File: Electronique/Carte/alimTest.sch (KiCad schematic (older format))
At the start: 20 parts

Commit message: Electronique
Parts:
- R4: value 1.7k -> 1.8k
- R5: value 2.1k -> 2.4k
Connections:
- net +15V renamed +20V
- net +15V_P renamed +20V_P
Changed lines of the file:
@@
 P 3150 5250
 F 0 "R4" V 3230 5250 50  0000 C CNN
-F 1 "1.7k" V 3150 5250 50  0000 C CNN
+F 1 "1.8k" V 3150 5250 50  0000 C CNN
 F 2 "Discret:R4" V 3080 5250 50  0001 C CNN
 F 3 "" H 3150 5250 50  0001 C CNN
@@
 P 5250 5250
 F 0 "R5" V 5330 5250 50  0000 C CNN
-F 1 "2.1k" V 5250 5250 50  0000 C CNN
+F 1 "2.4k" V 5250 5250 50  0000 C CNN
 F 2 "Discret:R4" V 5180 5250 50  0001 C CNN
 F 3 "" H 5250 5250 50  0001 C CNN
@@
 $EndComp
 Text GLabel 5700 4650 1    60   Input ~ 0
-+15V
++20V
 Text GLabel 4350 5250 0    60   Input ~ 0
 GND
 Text GLabel 5700 5500 3    60   Input ~ 0
-+15V_P
++20V_P
 Wire Wire Line
 	4350 5250 4650 5250

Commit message: kicadFinal
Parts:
- R5: value 2.4k -> 1.8k
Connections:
- net +20V renamed +15V
- net +20V_P renamed +15V_P
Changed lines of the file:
@@
 EESchema Schematic File Version 2
-LIBS:1A_cdfr2017
-LIBS:1A_cdfr2017-rescue
-LIBS:1A_cdfr2017-cache
 LIBS:power
 LIBS:device
@@
 LIBS:mcp2562
 LIBS:dsn2596
+LIBS:1A_cdfr2017
+LIBS:central-cache
+LIBS:central-rescue
 LIBS:carte_1A_cdfr2018-cache
 EELAYER 25 0
@@
 $Descr A4 11693 8268
 encoding utf-8
-Sheet 2 3
+Sheet 2 4
 Title ""
 Date ""
@@
 	3050 3750 3450 3750
 $Comp
-L PWR_FLAG #FLG06
+L PWR_FLAG #FLG028
 U 1 1 591A32A2
 P 3750 3650
-F 0 "#FLG06" H 3750 3725 50  0001 C CNN
+F 0 "#FLG028" H 3750 3725 50  0001 C CNN
 F 1 "PWR_FLAG" H 3750 3800 50  0000 C CNN
 F 2 "" H 3750 3650 50  0001 C CNN
@@
 	5150 3750 5550 3750
 $Comp
-L PWR_FLAG #FLG07
+L PWR_FLAG #FLG029
 U 1 1 5A64E1BA
 P 5850 3650
-F 0 "#FLG07" H 5850 3725 50  0001 C CNN
+F 0 "#FLG029" H 5850 3725 50  0001 C CNN
 F 1 "PWR_FLAG" H 5850 3800 50  0000 C CNN
 F 2 "" H 5850 3650 50  0001 C CNN
@@
 	7250 3750 7650 3750
 $Comp
-L PWR_FLAG #FLG08
+L PWR_FLAG #FLG030
 U 1 1 5A64E3A9
 P 7950 3650
-F 0 "#FLG08" H 7950 3725 50  0001 C CNN
+F 0 "#FLG030" H 7950 3725 50  0001 C CNN
 F 1 "PWR_FLAG" H 7950 3800 50  0000 C CNN
 F 2 "" H 7950 3650 50  0001 C CNN
@@
 	3050 5450 3450 5450
 $Comp
-L PWR_FLAG #FLG?
+L PWR_FLAG #FLG031
 U 1 1 5AC0B972
 P 3750 5350
-F 0 "#FLG?" H 3750 5425 50  0001 C CNN
+F 0 "#FLG031" H 3750 5425 50  0001 C CNN
 F 1 "PWR_FLAG" H 3750 5500 50  0000 C CNN
 F 2 "" H 3750 5350 50  0001 C CNN
@@
 P 5250 5250
 F 0 "R5" V 5330 5250 50  0000 C CNN
-F 1 "2.4k" V 5250 5250 50  0000 C CNN
+F 1 "1.8k" V 5250 5250 50  0000 C CNN
 F 2 "Discret:R4" V 5180 5250 50  0001 C CNN
 F 3 "" H 5250 5250 50  0001 C CNN
@@
 $EndComp
 Text GLabel 5700 4650 1    60   Input ~ 0
-+20V
++15V
 Text GLabel 4350 5250 0    60   Input ~ 0
 GND
 Text GLabel 5700 5500 3    60   Input ~ 0
-+20V_P
++15V_P
 Wire Wire Line
 	4350 5250 4650 5250
@@
 	5150 5450 5550 5450
 $Comp
-L PWR_FLAG #FLG?
+L PWR_FLAG #FLG032
 U 1 1 5AC0BAE9
 P 5850 5350
-F 0 "#FLG?" H 5850 5425 50  0001 C CNN
+F 0 "#FLG032" H 5850 5425 50  0001 C CNN
 F 1 "PWR_FLAG" H 5850 5500 50  0000 C CNN
 F 2 "" H 5850 5350 50  0001 C CNN

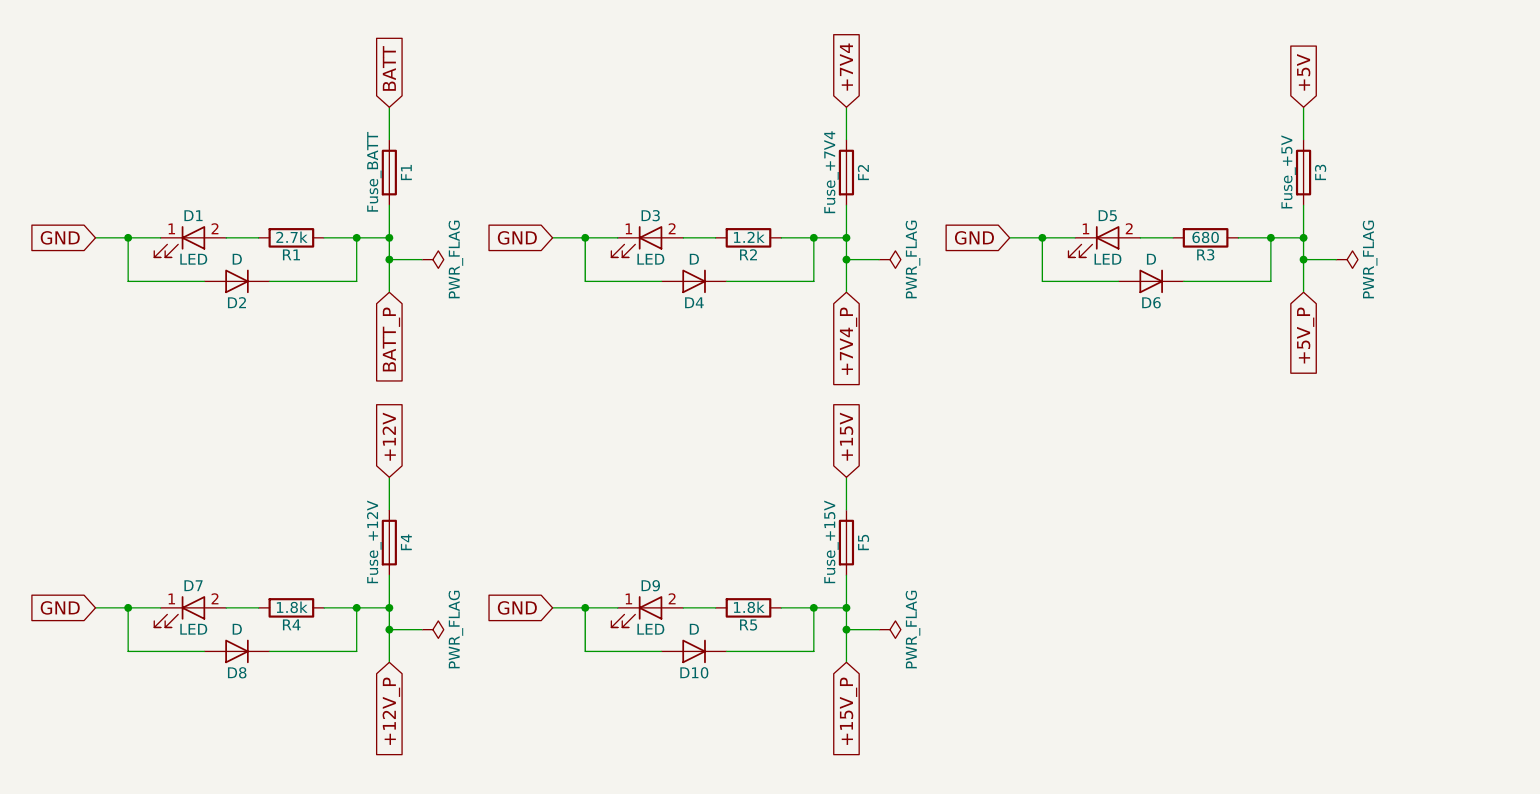
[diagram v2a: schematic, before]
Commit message: rapide corretion des empreintes pour les servos
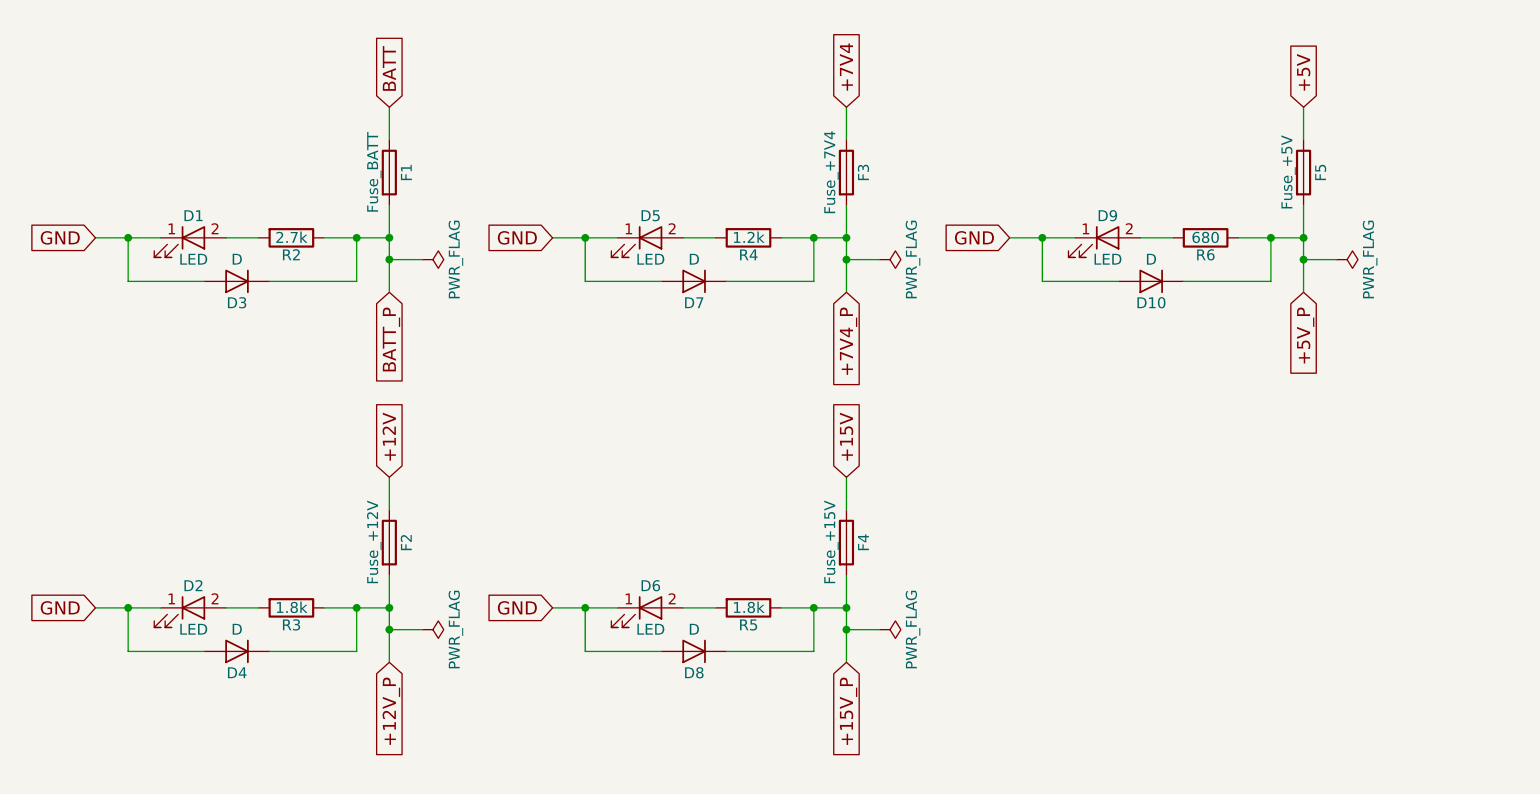
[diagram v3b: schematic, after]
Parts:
- renumbered D6 to D10, D7 to D2, D2 to D3, D8 to D4, D3 to D5, D9 to D6, D4 to D7, D10 to D8, D5 to D9, F4 to F2, F2 to F3, F5 to F4, F3 to F5, R1 to R2, R4 to R3, R2 to R4, R3 to R6
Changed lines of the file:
@@
 $EndComp
 $Comp
-L R R1
+L R R2
 U 1 1 5916B62D
 P 3150 3550
-F 0 "R1" V 3230 3550 50  0000 C CNN
+F 0 "R2" V 3230 3550 50  0000 C CNN
 F 1 "2.7k" V 3150 3550 50  0000 C CNN
 F 2 "Discret:R4" V 3080 3550 50  0001 C CNN
@@
 Connection ~ 3600 3550
 $Comp
-L D D2
+L D D3
 U 1 1 5916B9FB
 P 2900 3750
-F 0 "D2" H 2900 3850 50  0000 C CNN
+F 0 "D3" H 2900 3850 50  0000 C CNN
 F 1 "D" H 2900 3650 50  0000 C CNN
 F 2 "Discret:D4" H 2900 3750 50  0001 C CNN
@@
 	3050 3750 3450 3750
 $Comp
-L PWR_FLAG #FLG028
+L PWR_FLAG #FLG21
 U 1 1 591A32A2
 P 3750 3650
-F 0 "#FLG028" H 3750 3725 50  0001 C CNN
+F 0 "#FLG21" H 3750 3725 50  0001 C CNN
 F 1 "PWR_FLAG" H 3750 3800 50  0000 C CNN
 F 2 "" H 3750 3650 50  0001 C CNN
@@
 	3600 3400 3600 3800
 $Comp
-L Fuse F2
+L Fuse F3
 U 1 1 5A64E198
 P 5700 3250
-F 0 "F2" V 5780 3250 50  0000 C CNN
+F 0 "F3" V 5780 3250 50  0000 C CNN
 F 1 "Fuse_+7V4" V 5625 3250 50  0000 C CNN
 F 2 "Fuse_Holders_and_Fuses:Fuseholder5x20_horiz_SemiClosed_Casing10x25mm" V 5630 3250 50  0001 C CNN
@@
 $EndComp
 $Comp
-L LED-RESCUE-carte_centrale D3
+L LED-RESCUE-carte_centrale D5
 U 1 1 5A64E19E
 P 4800 3550
-F 0 "D3" H 4800 3650 50  0000 C CNN
+F 0 "D5" H 4800 3650 50  0000 C CNN
 F 1 "LED" H 4800 3450 50  0000 C CNN
 F 2 "LEDs:LED_D5.0mm" H 4800 3550 50  0001 C CNN
@@
 $EndComp
 $Comp
-L R R2
+L R R4
 U 1 1 5A64E1A4
 P 5250 3550
-F 0 "R2" V 5330 3550 50  0000 C CNN
+F 0 "R4" V 5330 3550 50  0000 C CNN
 F 1 "1.2k" V 5250 3550 50  0000 C CNN
 F 2 "Discret:R4" V 5180 3550 50  0001 C CNN
@@
 Connection ~ 5700 3550
 $Comp
-L D D4
+L D D7
 U 1 1 5A64E1B0
 P 5000 3750
-F 0 "D4" H 5000 3850 50  0000 C CNN
+F 0 "D7" H 5000 3850 50  0000 C CNN
 F 1 "D" H 5000 3650 50  0000 C CNN
 F 2 "Discret:D4" H 5000 3750 50  0001 C CNN
@@
 	5150 3750 5550 3750
 $Comp
-L PWR_FLAG #FLG029
+L PWR_FLAG #FLG23
 U 1 1 5A64E1BA
 P 5850 3650
-F 0 "#FLG029" H 5850 3725 50  0001 C CNN
+F 0 "#FLG23" H 5850 3725 50  0001 C CNN
 F 1 "PWR_FLAG" H 5850 3800 50  0000 C CNN
 F 2 "" H 5850 3650 50  0001 C CNN
@@
 	5700 3400 5700 3800
 $Comp
-L Fuse F3
+L Fuse F5
 U 1 1 5A64E387
 P 7800 3250
-F 0 "F3" V 7880 3250 50  0000 C CNN
+F 0 "F5" V 7880 3250 50  0000 C CNN
 F 1 "Fuse_+5V" V 7725 3250 50  0000 C CNN
 F 2 "Fuse_Holders_and_Fuses:Fuseholder5x20_horiz_SemiClosed_Casing10x25mm" V 7730 3250 50  0001 C CNN
@@
 $EndComp
 $Comp
-L LED-RESCUE-carte_centrale D5
+L LED-RESCUE-carte_centrale D9
 U 1 1 5A64E38D
 P 6900 3550
-F 0 "D5" H 6900 3650 50  0000 C CNN
+F 0 "D9" H 6900 3650 50  0000 C CNN
 F 1 "LED" H 6900 3450 50  0000 C CNN
 F 2 "LEDs:LED_D5.0mm" H 6900 3550 50  0001 C CNN
@@
 $EndComp
 $Comp
-L R R3
+L R R6
 U 1 1 5A64E393
 P 7350 3550
-F 0 "R3" V 7430 3550 50  0000 C CNN
+F 0 "R6" V 7430 3550 50  0000 C CNN
 F 1 "680" V 7350 3550 50  0000 C CNN
 F 2 "Discret:R4" V 7280 3550 50  0001 C CNN
@@
 Connection ~ 7800 3550
 $Comp
-L D D6
+L D D10
 U 1 1 5A64E39F
 P 7100 3750
-F 0 "D6" H 7100 3850 50  0000 C CNN
+F 0 "D10" H 7100 3850 50  0000 C CNN
 F 1 "D" H 7100 3650 50  0000 C CNN
 F 2 "Discret:D4" H 7100 3750 50  0001 C CNN
@@
 	7250 3750 7650 3750
 $Comp
-L PWR_FLAG #FLG030
+L PWR_FLAG #FLG25
 U 1 1 5A64E3A9
 P 7950 3650
-F 0 "#FLG030" H 7950 3725 50  0001 C CNN
+F 0 "#FLG25" H 7950 3725 50  0001 C CNN
 F 1 "PWR_FLAG" H 7950 3800 50  0000 C CNN
 F 2 "" H 7950 3650 50  0001 C CNN
@@
 	7800 3400 7800 3800
 $Comp
-L Fuse F4
+L Fuse F2
 U 1 1 5AC0B950
 P 3600 4950
-F 0 "F4" V 3680 4950 50  0000 C CNN
+F 0 "F2" V 3680 4950 50  0000 C CNN
 F 1 "Fuse_+12V" V 3525 4950 50  0000 C CNN
 F 2 "Fuse_Holders_and_Fuses:Fuseholder5x20_horiz_SemiClosed_Casing10x25mm" V 3530 4950 50  0001 C CNN
@@
 $EndComp
 $Comp
-L LED-RESCUE-carte_centrale D7
+L LED-RESCUE-carte_centrale D2
 U 1 1 5AC0B956
 P 2700 5250
-F 0 "D7" H 2700 5350 50  0000 C CNN
+F 0 "D2" H 2700 5350 50  0000 C CNN
 F 1 "LED" H 2700 5150 50  0000 C CNN
 F 2 "LEDs:LED_D5.0mm" H 2700 5250 50  0001 C CNN
@@
 $EndComp
 $Comp
-L R R4
+L R R3
 U 1 1 5AC0B95C
 P 3150 5250
-F 0 "R4" V 3230 5250 50  0000 C CNN
+F 0 "R3" V 3230 5250 50  0000 C CNN
 F 1 "1.8k" V 3150 5250 50  0000 C CNN
 F 2 "Discret:R4" V 3080 5250 50  0001 C CNN
@@
 Connection ~ 3600 5250
 $Comp
-L D D8
+L D D4
 U 1 1 5AC0B968
 P 2900 5450
-F 0 "D8" H 2900 5550 50  0000 C CNN
+F 0 "D4" H 2900 5550 50  0000 C CNN
 F 1 "D" H 2900 5350 50  0000 C CNN
 F 2 "Discret:D4" H 2900 5450 50  0001 C CNN
@@
 	3050 5450 3450 5450
 $Comp
-L PWR_FLAG #FLG031
+L PWR_FLAG #FLG22
 U 1 1 5AC0B972
 P 3750 5350
-F 0 "#FLG031" H 3750 5425 50  0001 C CNN
+F 0 "#FLG22" H 3750 5425 50  0001 C CNN
 F 1 "PWR_FLAG" H 3750 5500 50  0000 C CNN
 F 2 "" H 3750 5350 50  0001 C CNN
@@
 	3600 5100 3600 5500
 $Comp
-L Fuse F5
+L Fuse F4
 U 1 1 5AC0BAC7
 P 5700 4950
-F 0 "F5" V 5780 4950 50  0000 C CNN
+F 0 "F4" V 5780 4950 50  0000 C CNN
 F 1 "Fuse_+15V" V 5625 4950 50  0000 C CNN
 F 2 "Fuse_Holders_and_Fuses:Fuseholder5x20_horiz_SemiClosed_Casing10x25mm" V 5630 4950 50  0001 C CNN
@@
 $EndComp
 $Comp
-L LED-RESCUE-carte_centrale D9
+L LED-RESCUE-carte_centrale D6
 U 1 1 5AC0BACD
 P 4800 5250
-F 0 "D9" H 4800 5350 50  0000 C CNN
+F 0 "D6" H 4800 5350 50  0000 C CNN
 F 1 "LED" H 4800 5150 50  0000 C CNN
 F 2 "LEDs:LED_D5.0mm" H 4800 5250 50  0001 C CNN
@@
 Connection ~ 5700 5250
 $Comp
-L D D10
+L D D8
 U 1 1 5AC0BADF
 P 5000 5450
-F 0 "D10" H 5000 5550 50  0000 C CNN
+F 0 "D8" H 5000 5550 50  0000 C CNN
 F 1 "D" H 5000 5350 50  0000 C CNN
 F 2 "Discret:D4" H 5000 5450 50  0001 C CNN
@@
 	5150 5450 5550 5450
 $Comp
-L PWR_FLAG #FLG032
+L PWR_FLAG #FLG24
 U 1 1 5AC0BAE9
 P 5850 5350
-F 0 "#FLG032" H 5850 5425 50  0001 C CNN
+F 0 "#FLG24" H 5850 5425 50  0001 C CNN
 F 1 "PWR_FLAG" H 5850 5500 50  0000 C CNN
 F 2 "" H 5850 5350 50  0001 C CNN

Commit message: correction
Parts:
- D10, D3, D4, D7, D8: footprint Discret:D4 -> Diodes_SMD:D_SMA_Handsoldering
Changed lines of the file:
@@
 F 0 "D3" H 2900 3850 50  0000 C CNN
 F 1 "D" H 2900 3650 50  0000 C CNN
-F 2 "Discret:D4" H 2900 3750 50  0001 C CNN
+F 2 "Diodes_SMD:D_SMA_Handsoldering" H 2900 3750 50  0001 C CNN
 F 3 "" H 2900 3750 50  0001 C CNN
 	1    2900 3750
@@
 F 0 "D7" H 5000 3850 50  0000 C CNN
 F 1 "D" H 5000 3650 50  0000 C CNN
-F 2 "Discret:D4" H 5000 3750 50  0001 C CNN
+F 2 "Diodes_SMD:D_SMA_Handsoldering" H 5000 3750 50  0001 C CNN
 F 3 "" H 5000 3750 50  0001 C CNN
 	1    5000 3750
@@
 F 0 "D10" H 7100 3850 50  0000 C CNN
 F 1 "D" H 7100 3650 50  0000 C CNN
-F 2 "Discret:D4" H 7100 3750 50  0001 C CNN
+F 2 "Diodes_SMD:D_SMA_Handsoldering" H 7100 3750 50  0001 C CNN
 F 3 "" H 7100 3750 50  0001 C CNN
 	1    7100 3750
@@
 F 0 "D4" H 2900 5550 50  0000 C CNN
 F 1 "D" H 2900 5350 50  0000 C CNN
-F 2 "Discret:D4" H 2900 5450 50  0001 C CNN
+F 2 "Diodes_SMD:D_SMA_Handsoldering" H 2900 5450 50  0001 C CNN
 F 3 "" H 2900 5450 50  0001 C CNN
 	1    2900 5450
@@
 F 0 "D8" H 5000 5550 50  0000 C CNN
 F 1 "D" H 5000 5350 50  0000 C CNN
-F 2 "Discret:D4" H 5000 5450 50  0001 C CNN
+F 2 "Diodes_SMD:D_SMA_Handsoldering" H 5000 5450 50  0001 C CNN
 F 3 "" H 5000 5450 50  0001 C CNN
 	1    5000 5450

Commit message: Kicad Final enfin !!
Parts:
- added J7, J8, J9: Conn_01x02, Connectors_Molex:Molex_KK-6410-02_02x2.54mm_Straight, symbol Conn_01x02
- R2, R3, R4, R5, R6: footprint Discret:R4 -> Resistors_SMD:R_1206_HandSoldering
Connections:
- net +5V_P: now also J8.1 (Pin_1), J9.1 (Pin_1)
- net +7V4_P: now also J7.1 (Pin_1)
- net GND: now also J7.2 (Pin_2), J8.2 (Pin_2), J9.2 (Pin_2)
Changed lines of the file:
@@
 F 0 "R2" V 3230 3550 50  0000 C CNN
 F 1 "2.7k" V 3150 3550 50  0000 C CNN
-F 2 "Discret:R4" V 3080 3550 50  0001 C CNN
+F 2 "Resistors_SMD:R_1206_HandSoldering" V 3080 3550 50  0001 C CNN
 F 3 "" H 3150 3550 50  0001 C CNN
 	1    3150 3550
@@
 	3050 3750 3450 3750
 $Comp
-L PWR_FLAG #FLG21
+L PWR_FLAG #FLG26
 U 1 1 591A32A2
 P 3750 3650
-F 0 "#FLG21" H 3750 3725 50  0001 C CNN
+F 0 "#FLG26" H 3750 3725 50  0001 C CNN
 F 1 "PWR_FLAG" H 3750 3800 50  0000 C CNN
 F 2 "" H 3750 3650 50  0001 C CNN
@@
 F 0 "R4" V 5330 3550 50  0000 C CNN
 F 1 "1.2k" V 5250 3550 50  0000 C CNN
-F 2 "Discret:R4" V 5180 3550 50  0001 C CNN
+F 2 "Resistors_SMD:R_1206_HandSoldering" V 5180 3550 50  0001 C CNN
 F 3 "" H 5250 3550 50  0001 C CNN
 	1    5250 3550
@@
 	5150 3750 5550 3750
 $Comp
-L PWR_FLAG #FLG23
+L PWR_FLAG #FLG28
 U 1 1 5A64E1BA
 P 5850 3650
-F 0 "#FLG23" H 5850 3725 50  0001 C CNN
+F 0 "#FLG28" H 5850 3725 50  0001 C CNN
 F 1 "PWR_FLAG" H 5850 3800 50  0000 C CNN
 F 2 "" H 5850 3650 50  0001 C CNN
@@
 F 0 "R6" V 7430 3550 50  0000 C CNN
 F 1 "680" V 7350 3550 50  0000 C CNN
-F 2 "Discret:R4" V 7280 3550 50  0001 C CNN
+F 2 "Resistors_SMD:R_1206_HandSoldering" V 7280 3550 50  0001 C CNN
 F 3 "" H 7350 3550 50  0001 C CNN
 	1    7350 3550
@@
 	7250 3750 7650 3750
 $Comp
-L PWR_FLAG #FLG25
+L PWR_FLAG #FLG30
 U 1 1 5A64E3A9
 P 7950 3650
-F 0 "#FLG25" H 7950 3725 50  0001 C CNN
+F 0 "#FLG30" H 7950 3725 50  0001 C CNN
 F 1 "PWR_FLAG" H 7950 3800 50  0000 C CNN
 F 2 "" H 7950 3650 50  0001 C CNN
@@
 F 0 "R3" V 3230 5250 50  0000 C CNN
 F 1 "1.8k" V 3150 5250 50  0000 C CNN
-F 2 "Discret:R4" V 3080 5250 50  0001 C CNN
+F 2 "Resistors_SMD:R_1206_HandSoldering" V 3080 5250 50  0001 C CNN
 F 3 "" H 3150 5250 50  0001 C CNN
 	1    3150 5250
@@
 	3050 5450 3450 5450
 $Comp
-L PWR_FLAG #FLG22
+L PWR_FLAG #FLG27
 U 1 1 5AC0B972
 P 3750 5350
-F 0 "#FLG22" H 3750 5425 50  0001 C CNN
+F 0 "#FLG27" H 3750 5425 50  0001 C CNN
 F 1 "PWR_FLAG" H 3750 5500 50  0000 C CNN
 F 2 "" H 3750 5350 50  0001 C CNN
@@
 F 0 "R5" V 5330 5250 50  0000 C CNN
 F 1 "1.8k" V 5250 5250 50  0000 C CNN
-F 2 "Discret:R4" V 5180 5250 50  0001 C CNN
+F 2 "Resistors_SMD:R_1206_HandSoldering" V 5180 5250 50  0001 C CNN
 F 3 "" H 5250 5250 50  0001 C CNN
 	1    5250 5250
@@
 	5150 5450 5550 5450
 $Comp
-L PWR_FLAG #FLG24
+L PWR_FLAG #FLG29
 U 1 1 5AC0BAE9
 P 5850 5350
-F 0 "#FLG24" H 5850 5425 50  0001 C CNN
+F 0 "#FLG29" H 5850 5425 50  0001 C CNN
 F 1 "PWR_FLAG" H 5850 5500 50  0000 C CNN
 F 2 "" H 5850 5350 50  0001 C CNN
@@
 Wire Wire Line
 	5700 5100 5700 5500
+$Comp
+L Conn_01x02 J7
+U 1 1 5ACAF90E
+P 6450 3850
+F 0 "J7" H 6450 3950 50  0000 C CNN
+F 1 "Conn_01x02" H 6450 3650 50  0000 C CNN
+F 2 "Connectors_Molex:Molex_KK-6410-02_02x2.54mm_Straight" H 6450 3850 50  0001 C CNN
+F 3 "" H 6450 3850 50  0001 C CNN
+	1    6450 3850
+	1    0    0    -1
+$EndComp
+$Comp
+L Conn_01x02 J9
+U 1 1 5ACAFA14
+P 8550 3900
+F 0 "J9" H 8550 4000 50  0000 C CNN
+F 1 "Conn_01x02" H 8550 3700 50  0000 C CNN
+F 2 "Connectors_Molex:Molex_KK-6410-02_02x2.54mm_Straight" H 8550 3900 50  0001 C CNN
+F 3 "" H 8550 3900 50  0001 C CNN
+	1    8550 3900
+	1    0    0    -1
+$EndComp
+Wire Wire Line
+	5700 3750 5900 3750
+Wire Wire Line
+	5900 3750 5900 3850
+Wire Wire Line
+	5900 3850 6250 3850
+Wire Wire Line
+	7800 3750 8000 3750
+Wire Wire Line
+	8000 3750 8000 3900
+Wire Wire Line
+	8000 3900 8350 3900
+Connection ~ 7800 3750
+$Comp
+L GND #PWR11
+U 1 1 5ACAFB82
+P 6250 3950
+F 0 "#PWR11" H 6250 3700 50  0001 C CNN
+F 1 "GND" H 6250 3800 50  0000 C CNN
+F 2 "" H 6250 3950 50  0001 C CNN
+F 3 "" H 6250 3950 50  0001 C CNN
+	1    6250 3950
+	0    1    -1   0
+$EndComp
+$Comp
+L GND #PWR13
+U 1 1 5ACAFBF2
+P 8350 4000
+F 0 "#PWR13" H 8350 3750 50  0001 C CNN
+F 1 "GND" H 8350 3850 50  0000 C CNN
+F 2 "" H 8350 4000 50  0001 C CNN
+F 3 "" H 8350 4000 50  0001 C CNN
+	1    8350 4000
+	0    1    -1   0
+$EndComp
+Connection ~ 5700 3750
+$Comp
+L Conn_01x02 J8
+U 1 1 5ACB3837
+P 8100 4550
+F 0 "J8" H 8100 4650 50  0000 C CNN
+F 1 "Conn_01x02" V 8100 4350 50  0000 C CNN
+F 2 "Connectors_Molex:Molex_KK-6410-02_02x2.54mm_Straight" H 8100 4550 50  0001 C CNN
+F 3 "" H 8100 4550 50  0001 C CNN
+	1    8100 4550
+	0    1    1    0
+$EndComp
+$Comp
+L GND #PWR12
+U 1 1 5ACB383D
+P 8000 4350
+F 0 "#PWR12" H 8000 4100 50  0001 C CNN
+F 1 "GND" H 8000 4200 50  0000 C CNN
+F 2 "" H 8000 4350 50  0001 C CNN
+F 3 "" H 8000 4350 50  0001 C CNN
+	1    8000 4350
+	1    0    0    1
+$EndComp
+Wire Wire Line
+	8100 3900 8100 4350
+Connection ~ 8100 3900
 $EndSCHEMATC
